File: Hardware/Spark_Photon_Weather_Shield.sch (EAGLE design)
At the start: 39 parts, among them U2 3.3V MIC5219, U3 ALS-PT19, U4 MPL3115A2LGA8, U5 HTU21D

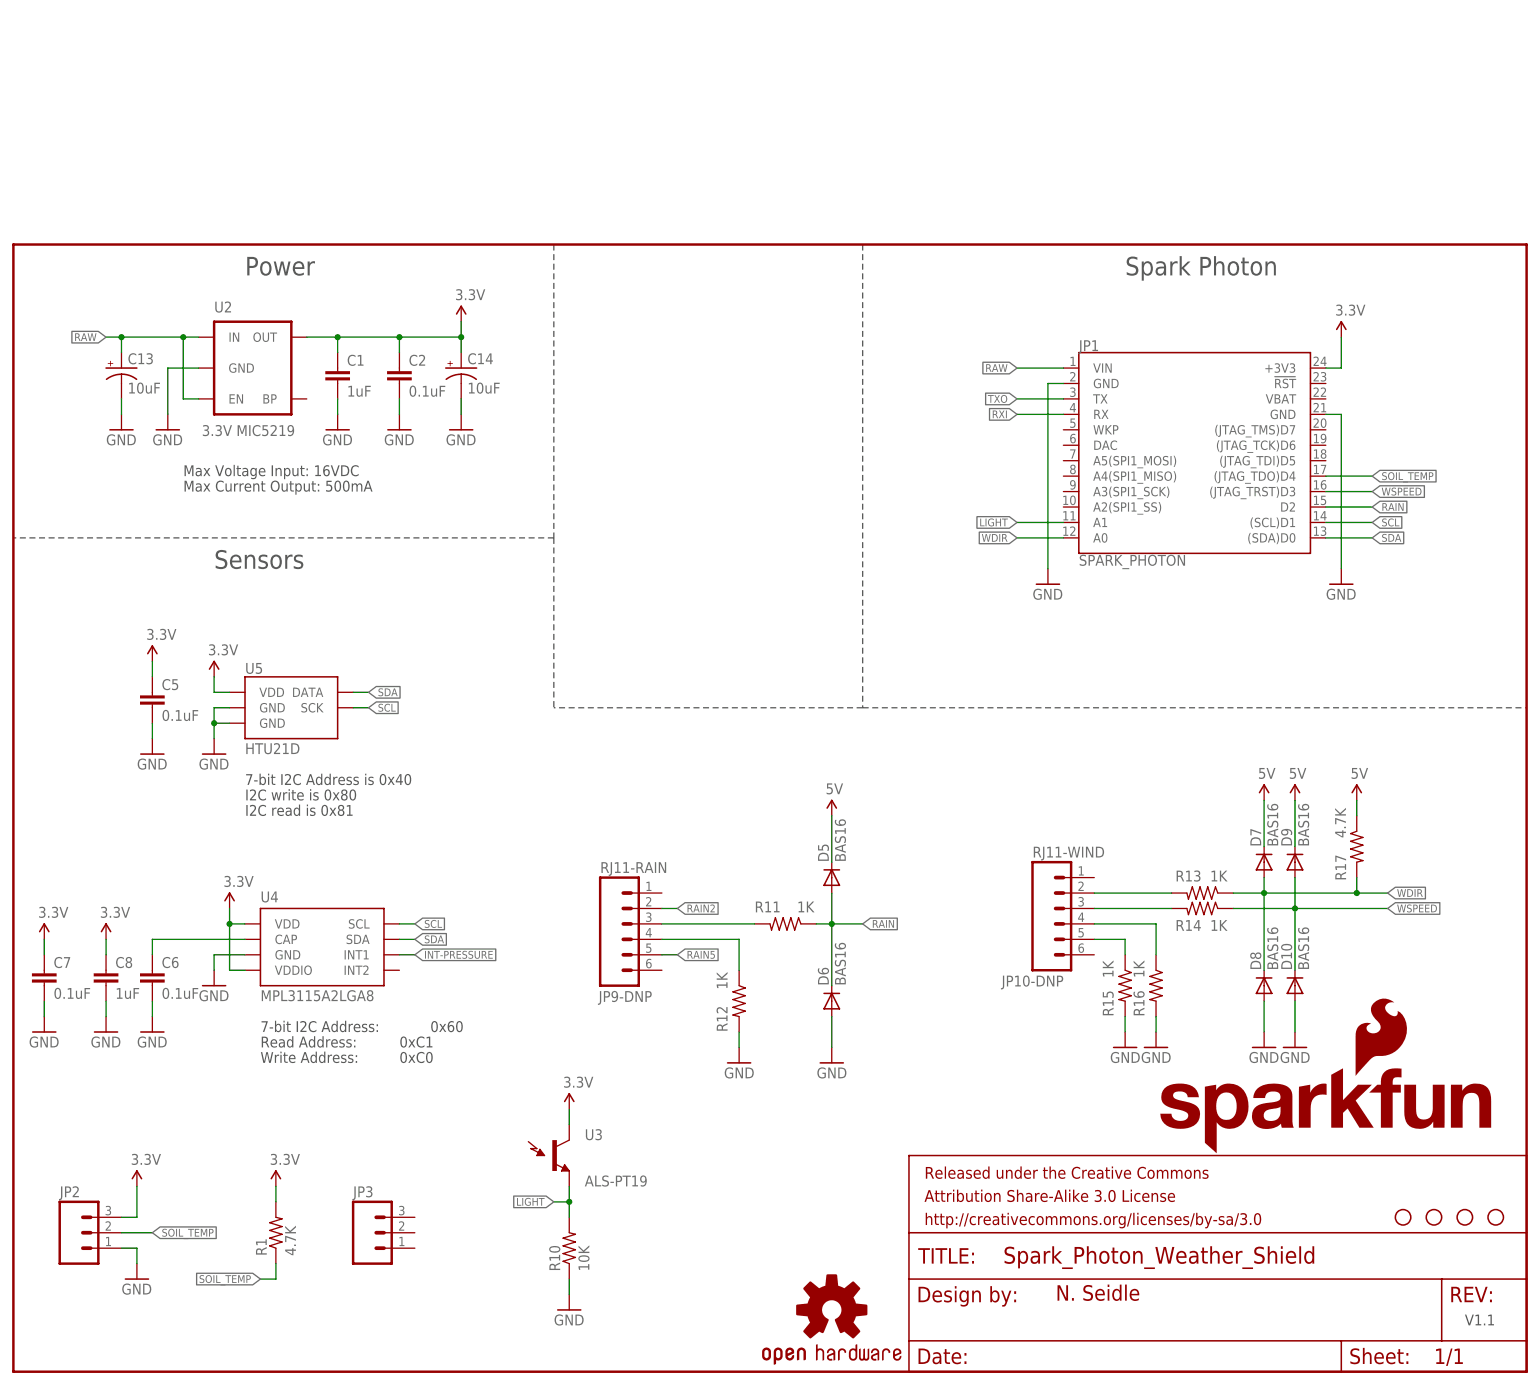
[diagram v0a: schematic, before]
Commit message: Adding I2C header
Adding I2C header to connect any I2C peripherals desired to enhance the
weather station.
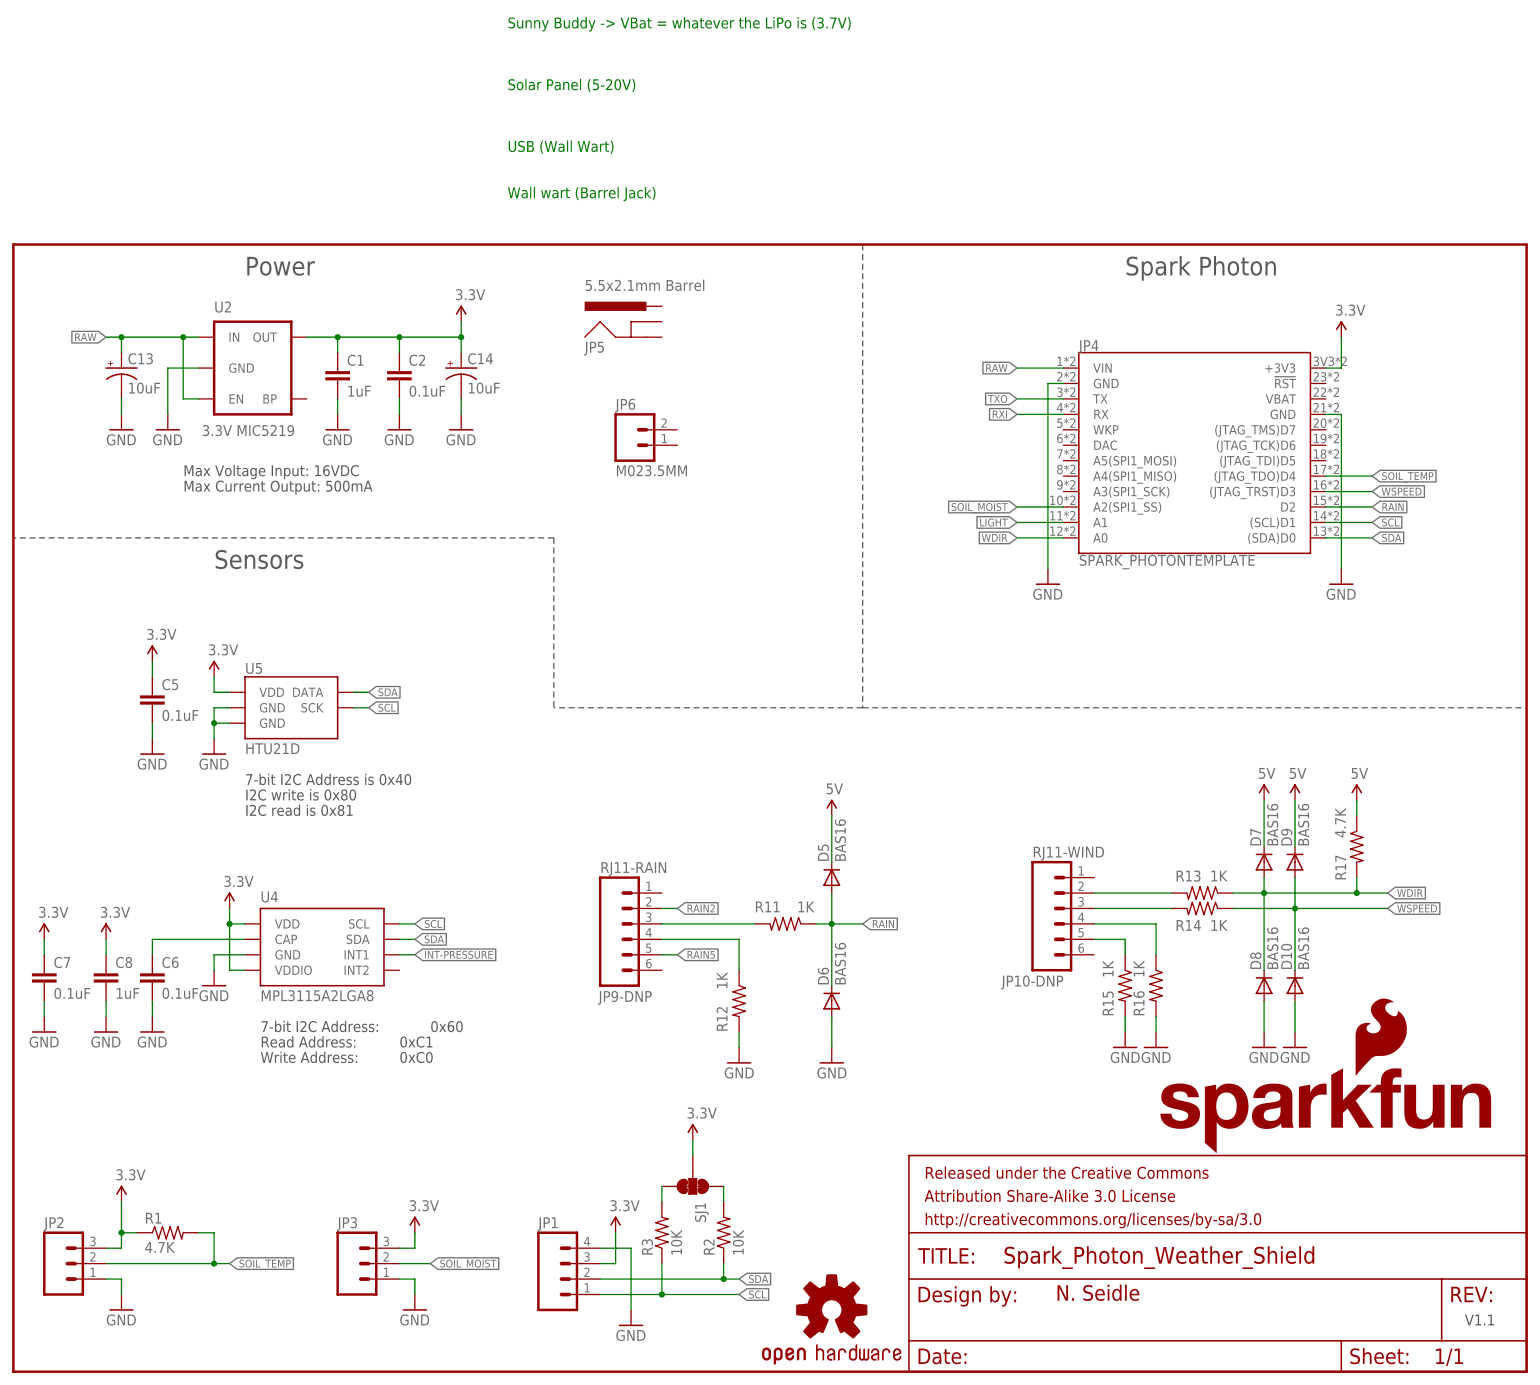
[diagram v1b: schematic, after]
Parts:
- removed R10: 10K, SparkFun-Passives:RESISTOR0603-RES
- removed STANDOFF1, STANDOFF2, STANDOFF3, STANDOFF4: STAND-OFF, SparkFun-Electromechanical:STAND-OFF
- removed U3: ALS-PT19, SparkFun-Sensors:LIGHTSENSORALS
- added JP4: SPARK_PHOTONTEMPLATE, template_temp:SPARK_PHOTONTEMPLATE
- added JP5: 5.5x2.1mm Barrel, SparkFun-Connectors:POWER_JACKSMD
- added JP6: M023.5MM, SparkFun-Connectors:M023.5MM
- added R2, R3: 10K, SparkFun-Resistors:10KOHM-1/10W-1%(0603)0603
- added SJ1: (no value), SparkFun-Passives:JUMPER-PAD-3-NC_BY_TRACE
- JP1: value SPARK_PHOTON -> (none); device template_temp:SPARK_PHOTON -> SparkFun-Connectors:M04PTH
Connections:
- new net N$3: R3.2, SJ1.3
- new net N$6: R2.2, SJ1.1
- new net SOIL_MOIST: JP3.2, JP4.A2(SPI1_SS)
- net 3.3V: now also JP4.+3V3; no longer JP1.+3V3, U3.C1
- net GND: now also JP1.4, JP3.1, JP4.GND@2, JP4.GND@21; no longer JP1.GND@2, JP1.GND@21, R10.1
- net LIGHT: now also JP4.A1; no longer JP1.A1, R10.2, U3.E1
- net RAIN: now also JP4.D2; no longer JP1.D2
- net RAW: now also JP4.VIN; no longer JP1.VIN
- net RXI: now also JP4.RX; no longer JP1.RX
- net SCL: now also JP1.1, JP4.(SCL)D1, R3.1; no longer JP1.(SCL)D1
- net SDA: now also JP1.2, JP4.(SDA)D0, R2.1; no longer JP1.(SDA)D0
- net SOIL_TEMP: now also JP4.(JTAG_TDO)D4, R1.2; no longer JP1.(JTAG_TDO)D4, R1.1
- net TXO: now also JP4.TX; no longer JP1.TX
- net VCC: now also JP1.3, JP3.3, R1.1, SJ1.2; no longer R1.2
- net WDIR: now also JP4.A0; no longer JP1.A0
- net WSPEED: now also JP4.(JTAG_TRST)D3; no longer JP1.(JTAG_TRST)D3
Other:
- note added: "I2C Connection"
- note added: "Soil Moisture"
- note added: "Solar Panel (5-20V)"
- note added: "Sunny Buddy -> VBat = whatever the LiPo is (3.7V)"
- note added: "USB (Wall Wart)"
- note added: "Wall wart (Barrel Jack)"
- note removed: "Light"
- moved on the sheet: JP2, JP3, R1

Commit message: Major Routing - Close to Proto
Major Routing - Close to Proto. added lots of silk and jumper features.
Finished routing.
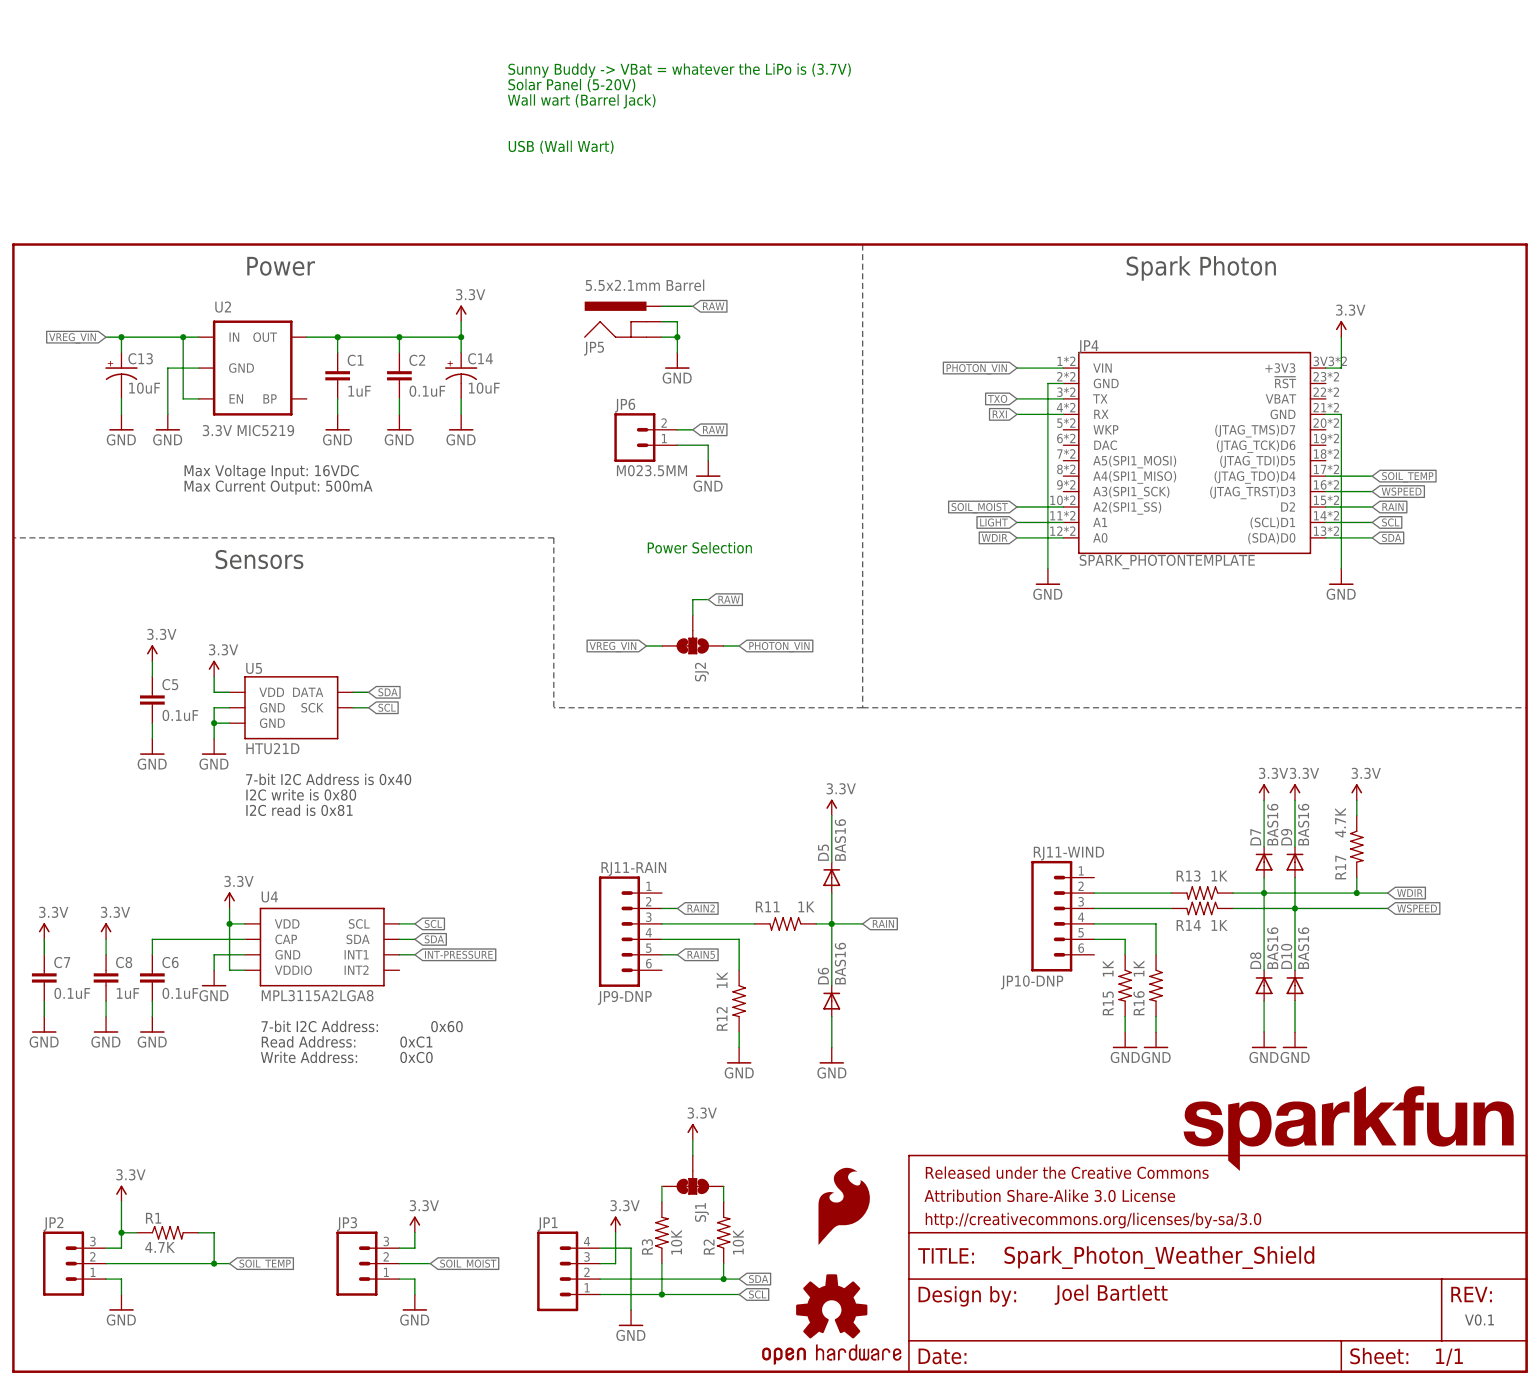
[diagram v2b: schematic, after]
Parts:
- removed LOGO2: SFE_LOGO_NAME_FLAME.1_INCH, SparkFun-Aesthetics:SFE_LOGO_NAME_FLAME.1_INCH
- added LOGO3: SFE_LOGO_NAME.1_INCH, SparkFun-Aesthetics:SFE_LOGO_NAME.1_INCH
- added LOGO4: SFE_LOGO_FLAME.2_INCH, SparkFun-Aesthetics:SFE_LOGO_FLAME.2_INCH
- added SJ2: JUMPER-PAD-3-2OF3_NC_BY_TRACE_SMALL, SparkFun-Passives:JUMPER-PAD-3-2OF3_NC_BY_TRACE_SMALL
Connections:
- removed net 5V: D5.C, D7.C, D9.C, R17.1
- removed net VCC: JP1.3, JP2.3, JP3.3, R1.1, SJ1.2
- new net PHOTON_VIN: JP4.VIN, SJ2.1
- new net VREG_VIN: C13.+, SJ2.3, U2.EN, U2.IN
- net 3.3V: now also D5.C, D7.C, D9.C, JP1.3, JP2.3, JP3.3, R1.1, R17.1, SJ1.2
- net GND: now also JP5.GND, JP5.GNDBREAK, JP6.1
- net RAW: now also JP5.PWR, JP6.2, SJ2.2; no longer C13.+, JP4.VIN, U2.EN, U2.IN
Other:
- note added: "Joel Bartlett"
- note added: "Power Selection"
- note added: "V0.1"
- note removed: "N. Seidle"
- note removed: "V1.1"

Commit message: Final touches before peer review
Ran my own QC checklist and fixed a few minor details such as
fiducials, labeling, more rerouting, etc.
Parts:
- removed LOGO3: SFE_LOGO_NAME.1_INCH, SparkFun-Aesthetics:SFE_LOGO_NAME.1_INCH
- removed LOGO4: SFE_LOGO_FLAME.2_INCH, SparkFun-Aesthetics:SFE_LOGO_FLAME.2_INCH
- removed U5: HTU21D, SparkFun-Sensors:HTU21DSMD
- added FID1, FID2: FIDUCIAL1X2, SparkFun-Aesthetics:FIDUCIAL1X2
- added LOGO2: SFE_LOGO_NAME_FLAME.1_INCH, SparkFun-Aesthetics:SFE_LOGO_NAME_FLAME.1_INCH
- added U1: 3.3V MIC5219, SparkFun:V_REG_LDOSMD
- FRAME2: value FRAME-LETTER -> (none); DESIGNER (none) -> Joel Bartlett
- U2: value 3.3V MIC5219 -> HTU21D; device SparkFun:V_REG_LDOSMD -> SparkFun-Sensors:HTU21DSMD
- renumbered JP10-DNP to JP8-DNP, JP9-DNP to JP7-DNP, U4 to U3
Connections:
- removed net VREG_VIN: C13.+, SJ2.3, U2.EN, U2.IN
- new net VREG: C13.+, SJ2.3, U1.EN, U1.IN
- net 3.3V: now also U1.OUT, U2.VDD; no longer U2.OUT, U5.VDD
- net GND: now also U1.GND, U2.GND@2, U2.GND@7; no longer U2.GND, U5.GND@2, U5.GND@7
- net SCL: now also U2.SCK; no longer U5.SCK
- net SDA: now also U2.DATA; no longer U5.DATA
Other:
- note added: "Based on the Weather Shield for Arduino by Nathan Seidle"
- note added: "I2C Port (optional)"
- note added: "Min Voltage Input: 5VDC"
- note added: "Photon Footprint"
- note added: "Soil Moisture (optional)"
- note added: "Soil/Water Temperature (optional)"
- note added: "USB (Wall Wart) w/ Micro USB"
- note added: "WAYS TO POWER:"
- note removed: "I2C Connection"
- note removed: "Joel Bartlett"
- note removed: "Soil Moisture"
- note removed: "Soil/Water Temperature"
- note removed: "Spark Photon"
- note removed: "USB (Wall Wart)"
- note removed: "V0.1"
- moved on the sheet: JP1, JP5, R2, R3, SJ1
